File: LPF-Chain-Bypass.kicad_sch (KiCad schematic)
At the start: 2 parts, among them K1 HK19F-DCxxV-SHC, K2 HK19F-DCxxV-SHC

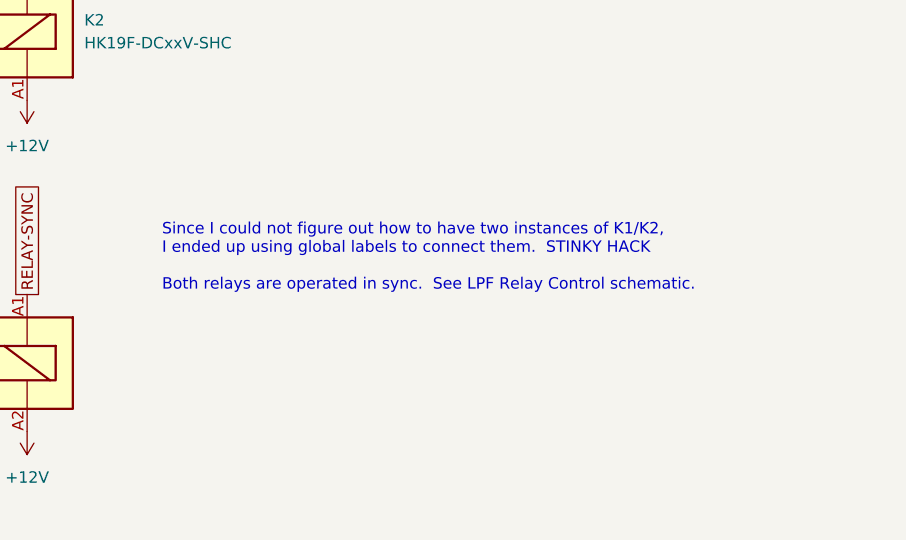
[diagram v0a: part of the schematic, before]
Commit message: v0.6 ERC passes.  I went over it with a fine tooth comb and corrected lots of little stuff.  Ron should review all the components I have to create very carefully.  In particular, MPS-751 symbol does not look correct.
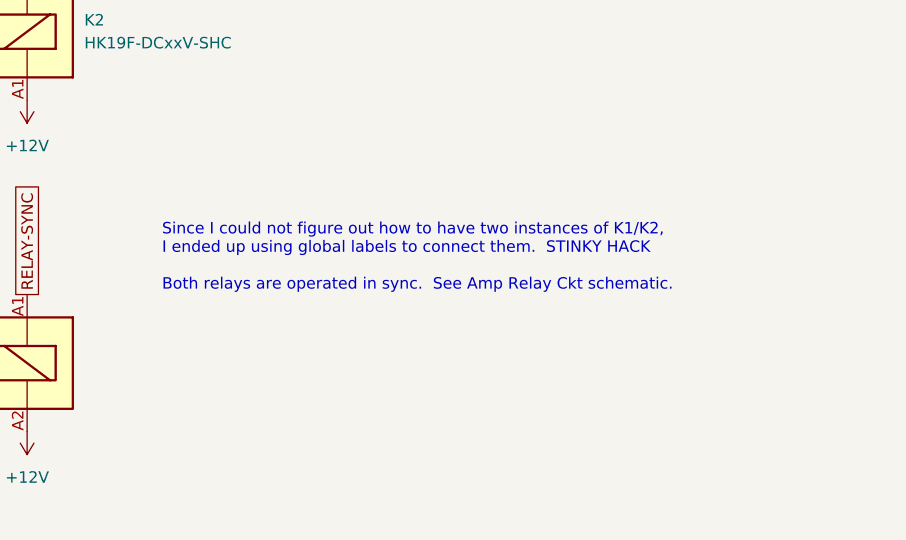
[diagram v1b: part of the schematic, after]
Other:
- note added: "Since I could not figure out how to have two instances of K1/K2, I ended up using global labels to connect them. STINKY HACK Both relays are operated in sync. See Amp Relay Ckt schematic."
- note removed: "Since I could not figure out how to have two instances of K1/K2, I ended up using global labels to connect them. STINKY HACK Both relays are operated in sync. See LPF Relay Control schematic."
- title: QMX Amp -> QMX+ Amp
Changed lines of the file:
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@@
 	(paper "USLetter")
 	(title_block
-		(title "QMX Amp")
-		(date "2024-08-12")
-		(rev "v0.5")
+		(title "QMX+ Amp")
+		(date "2024-08-13")
+		(rev "v0.6")
 		(company "WA7GIL")
 	)
@@
 		)
 	)
-	(text "Since I could not figure out how to have two instances of K1/K2,\nI ended up using global labels to connect them.  STINKY HACK\n\nBoth relays are operated in sync.  See LPF Relay Control schematic."
+	(text "Since I could not figure out how to have two instances of K1/K2,\nI ended up using global labels to connect them.  STINKY HACK\n\nBoth relays are operated in sync.  See Amp Relay Ckt schematic."
 		(exclude_from_sim no)
 		(at 166.116 96.266 0)

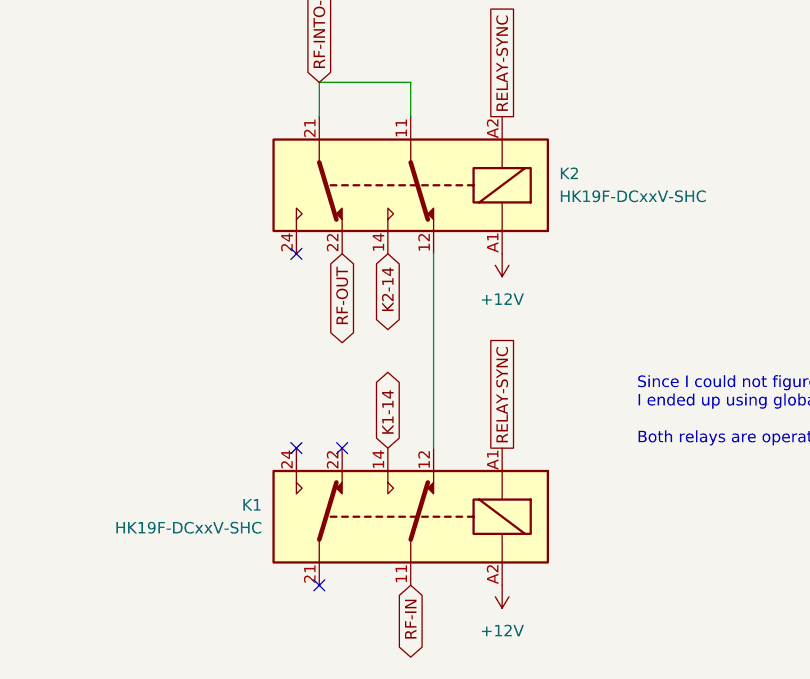
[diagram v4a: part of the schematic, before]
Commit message: expended to all 6 LPFs.  ERC pass.  Need to check component values on new LPF page
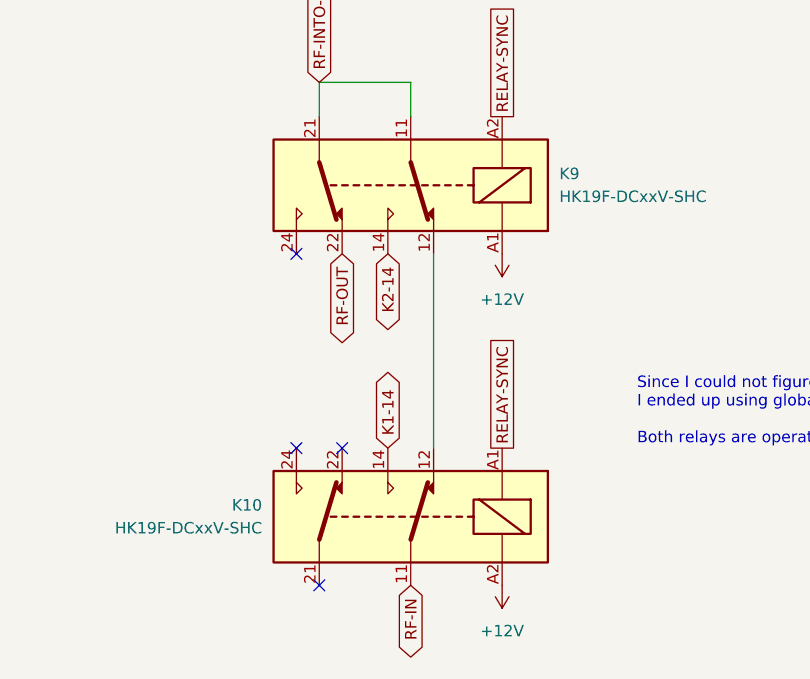
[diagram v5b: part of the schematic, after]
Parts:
- renumbered K1 to K10, K2 to K9
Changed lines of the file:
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@@
 		(dnp no)
 		(fields_autoplaced yes)
-		(property "Reference" "#PWR033"
+		(property "Reference" "#PWR031"
 			(at 151.13 111.76 0)
 			(effects
@@
 			(project ""
 				(path "/e63e39d7-6ac0-4ffd-8aa3-1841a4541b55/437da5b9-3c1b-43a3-b733-5d9a574d228b"
-					(reference "#PWR033")
+					(reference "#PWR031")
 					(unit 1)
 				)
@@
 		(dnp no)
 		(fields_autoplaced yes)
-		(property "Reference" "#PWR042"
+		(property "Reference" "#PWR030"
 			(at 151.13 74.93 0)
 			(effects
@@
 			(project "QMX-amp"
 				(path "/e63e39d7-6ac0-4ffd-8aa3-1841a4541b55/437da5b9-3c1b-43a3-b733-5d9a574d228b"
-					(reference "#PWR042")
+					(reference "#PWR030")
 					(unit 1)
 				)
@@
 		(dnp no)
 		(fields_autoplaced yes)
-		(property "Reference" "K2"
+		(property "Reference" "K9"
 			(at 157.48 69.8499 0)
 			(effects
@@
 			(project ""
 				(path "/e63e39d7-6ac0-4ffd-8aa3-1841a4541b55/437da5b9-3c1b-43a3-b733-5d9a574d228b"
-					(reference "K2")
+					(reference "K9")
 					(unit 1)
 				)
@@
 		(on_board yes)
 		(dnp no)
-		(property "Reference" "K1"
+		(property "Reference" "K10"
 			(at 124.46 106.6799 0)
 			(effects
@@
 			(project "QMX-amp"
 				(path "/e63e39d7-6ac0-4ffd-8aa3-1841a4541b55/437da5b9-3c1b-43a3-b733-5d9a574d228b"
-					(reference "K1")
-					(unit 1)
-				)
+					(reference "K10")
+					(unit 1)
+				)

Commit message: checkpoint before I shrink width of capps  so things might fit PCB
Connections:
- net K1-14 renamed K10-14
- net K2-14 renamed K9-14
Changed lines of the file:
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@@
 		(title "QMX+ Amp")
 		(date "2024-08-19")
-		(rev "v0.9")
+		(rev "v0.10")
 		(company "WA7GIL")
 	)
@@
 		)
 	)
-	(global_label "K2-14"
+	(global_label "K9-14"
 		(shape bidirectional)
 		(at 138.43 78.74 270)
@@
 		)
 	)
-	(global_label "K1-14"
+	(global_label "K10-14"
 		(shape bidirectional)
 		(at 138.43 100.33 90)
@@
 		)
 		(property "Intersheetrefs" "${INTERSHEET_REFS}"
-			(at 138.43 89.7628 90)
-			(effects
-				(font
+			(at 138.43 88.5533 90)
+			(effects
+				(font
